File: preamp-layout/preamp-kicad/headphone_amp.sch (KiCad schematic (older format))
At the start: 34 parts, among them J72 Conn_01x04_Male, J73 Conn_01x02_Male, J74 Conn_01x02_Male, J75 Conn_01x03_Male, J76 Conn_01x03_Male, J77 Conn_01x03_Male, J78 Conn_01x03_Female, J79 Conn_01x04_Male, U19 TL072, U20 TPA6120

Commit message: Schematic Updates
Updated pin connections for DAC, footprint updates, MCU connections.
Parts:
- C41, C42, C43, C44: footprint (none) -> Capacitor_SMD:C_0805_2012Metric_Pad1.15x1.40mm_HandSolder
- J72, J79: footprint (none) -> Connector_PinHeader_2.54mm:PinHeader_1x04_P2.54mm_Vertical
- J75, J78: footprint (none) -> Connector_PinHeader_2.54mm:PinHeader_1x03_P2.54mm_Vertical
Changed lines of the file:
@@
 F 0 "C41" H 5815 2546 50  0000 L CNN
 F 1 "0.001uF" H 5815 2455 50  0000 L CNN
-F 2 "" H 5738 2350 50  0001 C CNN
+F 2 "Capacitor_SMD:C_0805_2012Metric_Pad1.15x1.40mm_HandSolder" H 5738 2350 50  0001 C CNN
 F 3 "~" H 5700 2500 50  0001 C CNN
 	1    5700 2500
@@
 F 0 "C43" V 6302 2200 50  0000 C CNN
 F 1 "0.1uF" V 6211 2200 50  0000 C CNN
-F 2 "" H 6088 2050 50  0001 C CNN
+F 2 "Capacitor_SMD:C_0805_2012Metric_Pad1.15x1.40mm_HandSolder" H 6088 2050 50  0001 C CNN
 F 3 "~" H 6050 2200 50  0001 C CNN
 	1    6050 2200
@@
 F 0 "J75" H 2422 4478 50  0000 R CNN
 F 1 "Conn_01x03_Male" H 2422 4433 50  0001 R CNN
-F 2 "" H 2450 4500 50  0001 C CNN
+F 2 "Connector_PinHeader_2.54mm:PinHeader_1x03_P2.54mm_Vertical" H 2450 4500 50  0001 C CNN
 F 3 "~" H 2450 4500 50  0001 C CNN
 	1    2450 4500
@@
 F 0 "C42" H 5815 4646 50  0000 L CNN
 F 1 "0.001uF" H 5815 4555 50  0000 L CNN
-F 2 "" H 5738 4450 50  0001 C CNN
+F 2 "Capacitor_SMD:C_0805_2012Metric_Pad1.15x1.40mm_HandSolder" H 5738 4450 50  0001 C CNN
 F 3 "~" H 5700 4600 50  0001 C CNN
 	1    5700 4600
@@
 F 0 "C44" V 6302 4300 50  0000 C CNN
 F 1 "0.1uF" V 6211 4300 50  0000 C CNN
-F 2 "" H 6088 4150 50  0001 C CNN
+F 2 "Capacitor_SMD:C_0805_2012Metric_Pad1.15x1.40mm_HandSolder" H 6088 4150 50  0001 C CNN
 F 3 "~" H 6050 4300 50  0001 C CNN
 	1    6050 4300
@@
 F 0 "J78" H 3478 4480 50  0000 L CNN
 F 1 "Conn_01x03_Female" H 3478 4435 50  0001 L CNN
-F 2 "" H 3450 4500 50  0001 C CNN
+F 2 "Connector_PinHeader_2.54mm:PinHeader_1x03_P2.54mm_Vertical" H 3450 4500 50  0001 C CNN
 F 3 "~" H 3450 4500 50  0001 C CNN
 	1    3450 4500
@@
 F 0 "J72" H 1608 2639 50  0000 C CNN
 F 1 "Conn_01x04_Male" H 1608 2640 50  0001 C CNN
-F 2 "" H 1500 2450 50  0001 C CNN
+F 2 "Connector_PinHeader_2.54mm:PinHeader_1x04_P2.54mm_Vertical" H 1500 2450 50  0001 C CNN
 F 3 "~" H 1500 2450 50  0001 C CNN
 	1    1500 2450
@@
 F 0 "J79" H 4022 2378 50  0000 R CNN
 F 1 "Conn_01x04_Male" H 4158 2640 50  0001 C CNN
-F 2 "" H 4050 2450 50  0001 C CNN
+F 2 "Connector_PinHeader_2.54mm:PinHeader_1x04_P2.54mm_Vertical" H 4050 2450 50  0001 C CNN
 F 3 "~" H 4050 2450 50  0001 C CNN
 	1    4050 2450

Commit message: Schematic Redesignation
Regenerated RefDes for all parts, updated BOM accordingly and perfomred check on values, RefDes present from schematic to BOM. Value changes, BOM filled in as a result.
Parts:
- removed J73, J74: Conn_01x02_Male, Connector_JST:JST_EH_B2B-EH-A_1x02_P2.50mm_Vertical, symbol Connector:Conn_01x02_Male
- removed J79: Conn_01x04_Male, Connector_PinHeader_2.54mm:PinHeader_1x04_P2.54mm_Vertical, symbol Connector:Conn_01x04_Male
- added J77: Conn_01x04_Female, Connector_PinHeader_2.54mm:PinHeader_1x04_P2.54mm_Vertical, symbol Connector:Conn_01x04_Female
- R62, R63: value 1.3k -> 1.5k
- renumbered J76 to J73, J77 to J74, J78 to J76
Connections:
- net GND: now also J77.2 (Pin_2)
- net xfeed_out_l: now also J77.1 (Pin_1)
- net xfeed_out_r: now also J77.3 (Pin_3)
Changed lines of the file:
@@
 Text HLabel 2150 4300 0    50   UnSpc ~ 0
 L_IN
-$Comp
-L Connector:Conn_01x02_Male J?
-U 1 1 60B7C07D
-P 1950 6100
-AR Path="/5E5EF2D4/60B7C07D" Ref="J?"  Part="1"
-AR Path="/6009D432/60B7C07D" Ref="J?"  Part="1"
-AR Path="/5E4A803E/60B7C07D" Ref="J73"  Part="1"
-F 0 "J73" H 1922 6028 50  0000 R CNN
-F 1 "Conn_01x02_Male" H 1922 5983 50  0001 R CNN
-F 2 "Connector_JST:JST_EH_B2B-EH-A_1x02_P2.50mm_Vertical" H 1950 6100 50  0001 C CNN
-F 3 "~" H 1950 6100 50  0001 C CNN
-	1    1950 6100
-	-1   0    0    -1
-$EndComp
-Text GLabel 1550 6100 0    50   UnSpc ~ 0
-+5V
-Wire Wire Line
-	1750 6200 1550 6200
-Wire Wire Line
-	1550 6200 1550 6300
-Wire Wire Line
-	1750 6100 1550 6100
-$Comp
-L power:GND #PWR?
-U 1 1 64EC0170
-P 1550 6300
-AR Path="/5E26F6FE/64EC0170" Ref="#PWR?"  Part="1"
-AR Path="/5E4A803E/64EC0170" Ref="#PWR097"  Part="1"
-F 0 "#PWR097" H 1550 6050 50  0001 C CNN
-F 1 "GND" H 1555 6127 50  0000 C CNN
-F 2 "" H 1550 6300 50  0001 C CNN
-F 3 "" H 1550 6300 50  0001 C CNN
-	1    1550 6300
-	1    0    0    -1
-$EndComp
 Text GLabel 3850 6100 1    50   UnSpc ~ 0
 +15V
@@
 AR Path="/5E4A803E/5E3C1B26" Ref="R62"  Part="1"
 F 0 "R62" H 3920 6396 50  0000 L CNN
-F 1 "1.3k" H 3920 6305 50  0000 L CNN
+F 1 "1.5k" H 3920 6305 50  0000 L CNN
 F 2 "Resistor_SMD:R_1206_3216Metric_Pad1.42x1.75mm_HandSolder" V 3780 6350 50  0001 C CNN
 F 3 "~" H 3850 6350 50  0001 C CNN
@@
 AR Path="/5E4A803E/5E3C1B36" Ref="R63"  Part="1"
 F 0 "R63" H 4470 6396 50  0000 L CNN
-F 1 "1.3k" H 4470 6305 50  0000 L CNN
+F 1 "1.5k" H 4470 6305 50  0000 L CNN
 F 2 "Resistor_SMD:R_1206_3216Metric_Pad1.42x1.75mm_HandSolder" V 4330 6350 50  0001 C CNN
 F 3 "~" H 4400 6350 50  0001 C CNN
@@
 AR Path="/5E27B612/647A3EBE" Ref="J?"  Part="1"
 AR Path="/6009D432/647A3EBE" Ref="J?"  Part="1"
-AR Path="/5E4A803E/647A3EBE" Ref="J76"  Part="1"
-F 0 "J76" H 2922 6178 50  0000 R CNN
+AR Path="/5E4A803E/647A3EBE" Ref="J73"  Part="1"
+F 0 "J73" H 2922 6178 50  0000 R CNN
 F 1 "Conn_01x03_Male" H 2922 6133 50  0001 R CNN
 F 2 "Connector_JST:JST_EH_B3B-EH-A_1x03_P2.50mm_Vertical" H 2950 6200 50  0001 C CNN
@@
 AR Path="/5E2D8DA2/5F33E58A" Ref="J?"  Part="1"
 AR Path="/6009D432/5F33E58A" Ref="J?"  Part="1"
-AR Path="/5E4A803E/5F33E58A" Ref="J78"  Part="1"
-F 0 "J78" H 3478 4480 50  0000 L CNN
+AR Path="/5E4A803E/5F33E58A" Ref="J76"  Part="1"
+F 0 "J76" H 3478 4480 50  0000 L CNN
 F 1 "Conn_01x03_Female" H 3478 4435 50  0001 L CNN
 F 2 "Connector_PinHeader_2.54mm:PinHeader_1x03_P2.54mm_Vertical" H 3450 4500 50  0001 C CNN
@@
 Text GLabel 1700 2650 2    50   UnSpc ~ 0
 -15V
-$Comp
-L Connector:Conn_01x04_Male J79
-U 1 1 5E709DB6
-P 4050 2450
-F 0 "J79" H 4022 2378 50  0000 R CNN
-F 1 "Conn_01x04_Male" H 4158 2640 50  0001 C CNN
-F 2 "Connector_PinHeader_2.54mm:PinHeader_1x04_P2.54mm_Vertical" H 4050 2450 50  0001 C CNN
-F 3 "~" H 4050 2450 50  0001 C CNN
-	1    4050 2450
-	-1   0    0    -1
-$EndComp
 NoConn ~ 3850 2650
 $Comp
@@
 Text GLabel 6200 6850 3    50   UnSpc ~ 0
 -15V
-$Comp
-L Connector:Conn_01x02_Male J?
-U 1 1 5E79808C
-P 1950 6700
-AR Path="/5E5EF2D4/5E79808C" Ref="J?"  Part="1"
-AR Path="/6009D432/5E79808C" Ref="J?"  Part="1"
-AR Path="/5E4A803E/5E79808C" Ref="J74"  Part="1"
-F 0 "J74" H 1922 6628 50  0000 R CNN
-F 1 "Conn_01x02_Male" H 1922 6583 50  0001 R CNN
-F 2 "Connector_JST:JST_EH_B2B-EH-A_1x02_P2.50mm_Vertical" H 1950 6700 50  0001 C CNN
-F 3 "~" H 1950 6700 50  0001 C CNN
-	1    1950 6700
-	-1   0    0    -1
-$EndComp
-Text GLabel 1550 6700 0    50   UnSpc ~ 0
-+5V
-Wire Wire Line
-	1750 6800 1550 6800
-Wire Wire Line
-	1550 6800 1550 6900
-Wire Wire Line
-	1750 6700 1550 6700
-$Comp
-L power:GND #PWR?
-U 1 1 5E798096
-P 1550 6900
-AR Path="/5E26F6FE/5E798096" Ref="#PWR?"  Part="1"
-AR Path="/5E4A803E/5E798096" Ref="#PWR098"  Part="1"
-F 0 "#PWR098" H 1550 6650 50  0001 C CNN
-F 1 "GND" H 1555 6727 50  0000 C CNN
-F 2 "" H 1550 6900 50  0001 C CNN
-F 3 "" H 1550 6900 50  0001 C CNN
-	1    1550 6900
-	1    0    0    -1
-$EndComp
 $Comp
 L power:GND #PWR?
@@
 AR Path="/5E27B612/5E7A75D4" Ref="J?"  Part="1"
 AR Path="/6009D432/5E7A75D4" Ref="J?"  Part="1"
-AR Path="/5E4A803E/5E7A75D4" Ref="J77"  Part="1"
-F 0 "J77" H 2922 6778 50  0000 R CNN
+AR Path="/5E4A803E/5E7A75D4" Ref="J74"  Part="1"
+F 0 "J74" H 2922 6778 50  0000 R CNN
 F 1 "Conn_01x03_Male" H 2922 6733 50  0001 R CNN
 F 2 "Connector_JST:JST_EH_B3B-EH-A_1x03_P2.50mm_Vertical" H 2950 6800 50  0001 C CNN
@@
 Text GLabel 2650 6600 0    50   UnSpc ~ 0
 +15V
+$Comp
+L Connector:Conn_01x04_Female J77
+U 1 1 5EF5CC6D
+P 4050 2450
+F 0 "J77" H 4078 2380 50  0000 L CNN
+F 1 "Conn_01x04_Female" H 4078 2335 50  0001 L CNN
+F 2 "Connector_PinHeader_2.54mm:PinHeader_1x04_P2.54mm_Vertical" H 4050 2450 50  0001 C CNN
+F 3 "~" H 4050 2450 50  0001 C CNN
+	1    4050 2450
+	1    0    0    -1
+$EndComp
 $EndSCHEMATC

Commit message: Added Bypass Capacitors
0.1uF caps added at power supplies of all ICs
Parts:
- added C61, C62, C63, C64, C65, C66: 0.1uF, Capacitor_SMD:C_0805_2012Metric_Pad1.15x1.40mm_HandSolder, symbol Device:C
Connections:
- net +15V: now also C61.1, C63.1, C65.1
- net -15V: now also C62.1, C64.1, C66.1
- net GND: now also C61.2, C62.2, C63.2, C64.2, C65.2, C66.2
- net at R72.1, R76.2: now also U20.5 (-); no longer U20.4 (+)
- net at R74.1: now also U20.4 (+); no longer U20.5 (-)
- net at U20.16 (-): now also R73.1, R77.2; no longer R75.1
- new net: R75.1, U20.17 (+)
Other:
- moved on the sheet: C41, C42, C43, C44, D57, D58, J73, J74, R62, R63, R64, R65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

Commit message: Footprint assignment updates
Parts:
- U19: footprint (none) -> Package_DIP:DIP-8_W7.62mm_Socket_LongPads
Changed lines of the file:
@@
 F 0 "U19" H 3908 6596 50  0000 L CNN
 F 1 "TL072" H 3908 6505 50  0000 L CNN
-F 2 "" H 3950 6550 50  0001 C CNN
+F 2 "Package_DIP:DIP-8_W7.62mm_Socket_LongPads" H 3950 6550 50  0001 C CNN
 F 3 "http://www.ti.com/lit/ds/symlink/tl071.pdf" H 3950 6550 50  0001 C CNN
 	3    3950 6550

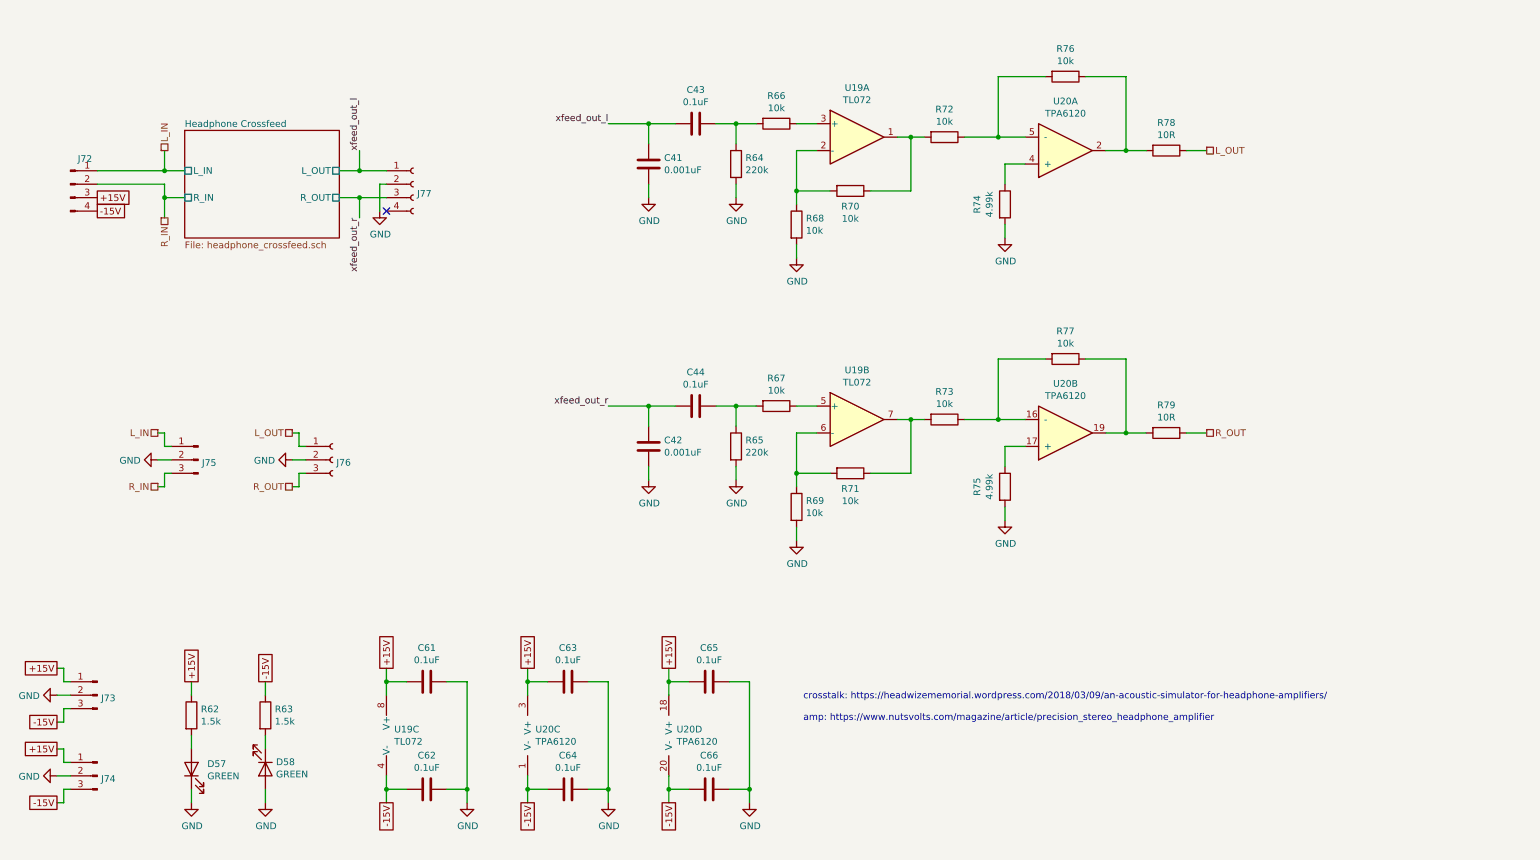
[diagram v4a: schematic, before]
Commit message: Headphone Amp Update
Removed IC buffer on headphone amp schematic. Reconfigured connectors to crossfeed board so that input/output can be easily jumpered.
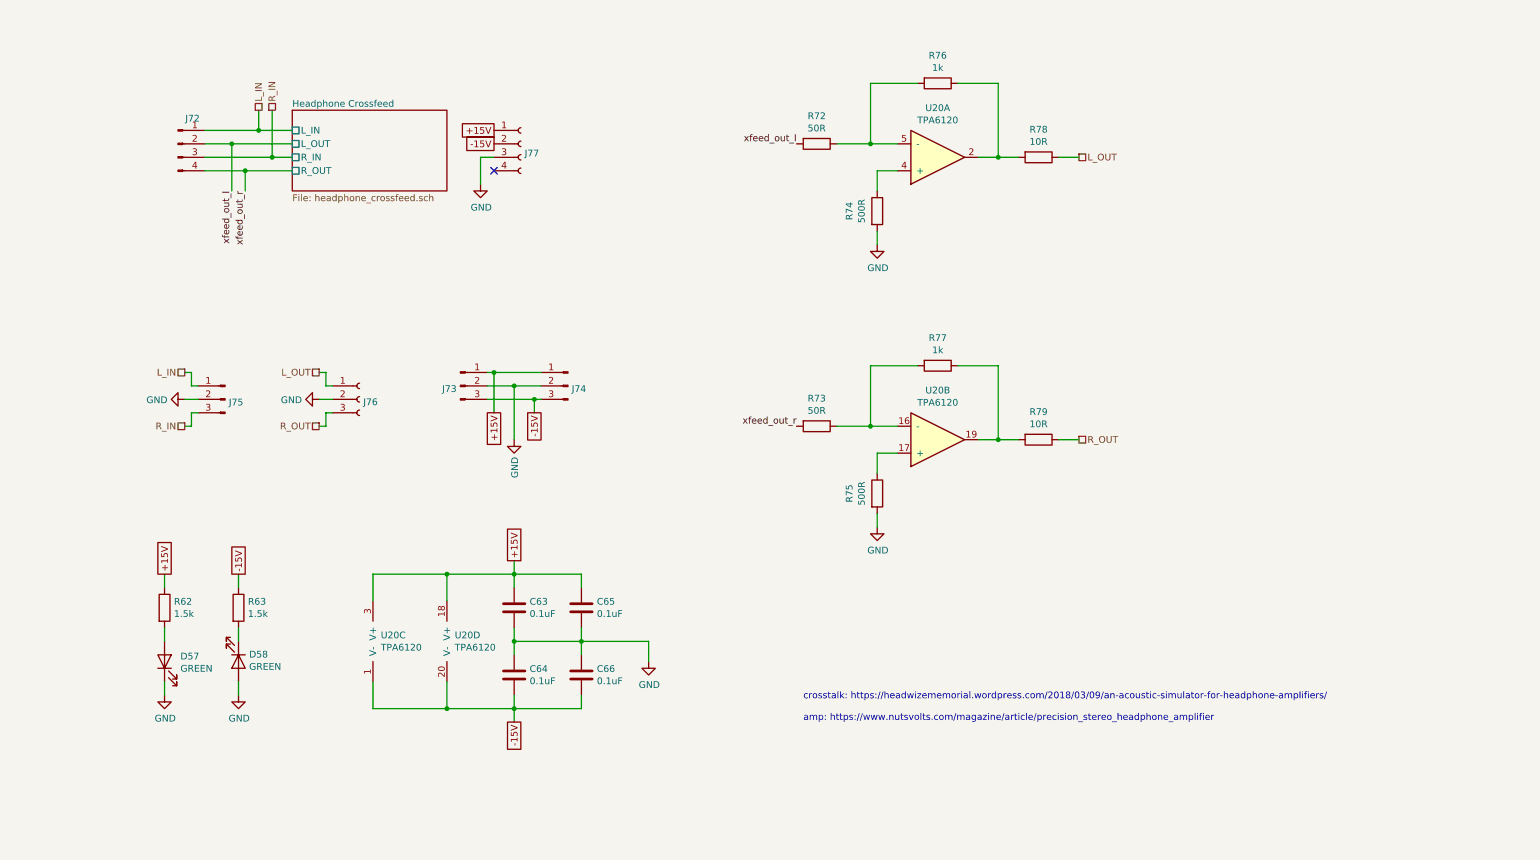
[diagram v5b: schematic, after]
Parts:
- removed C41, C42: 0.001uF, Capacitor_SMD:C_0805_2012Metric_Pad1.15x1.40mm_HandSolder, symbol Device:C
- removed C43, C44, C61, C62: 0.1uF, Capacitor_SMD:C_0805_2012Metric_Pad1.15x1.40mm_HandSolder, symbol Device:C
- removed R64, R65: 220k, Resistor_SMD:R_1206_3216Metric_Pad1.42x1.75mm_HandSolder, symbol Device:R
- removed R66, R67, R68, R69, R70, R71: 10k, Resistor_SMD:R_1206_3216Metric_Pad1.42x1.75mm_HandSolder, symbol Device:R
- removed U19: TL072, Package_DIP:DIP-8_W7.62mm_Socket_LongPads, symbol Amplifier_Operational:TL072
- R72, R73: value 10k -> 50R
- R74, R75: value 4.99k -> 500R
- R76, R77: value 10k -> 1k
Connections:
- net +15V: now also J77.1 (Pin_1); no longer J72.3 (Pin_3)
- net -15V: now also C66.2, J77.2 (Pin_2); no longer C66.1, J72.4 (Pin_4)
- net GND: now also C66.1, J77.3 (Pin_3); no longer C66.2, J77.2 (Pin_2)
- net R_IN: now also J72.3 (Pin_3); no longer J72.2 (Pin_2)
- net xfeed_out_l: now also J72.2 (Pin_2), R72.2; no longer J77.1 (Pin_1)
- net xfeed_out_r: now also J72.4 (Pin_4), R73.2; no longer J77.3 (Pin_3)
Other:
- moved on the sheet: C63, C64, C65, C66, D57, D58, J72, J73, J74, J75, J76, J77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

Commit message: Footprint updates
Footprint creation of relay, ESP32
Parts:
- U20: footprint (none) -> Package_SO:SOIC-20W_7.5x12.8mm_P1.27mm
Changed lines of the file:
@@
 F 0 "U20" H 3808 5896 50  0000 L CNN
 F 1 "TPA6120" H 3808 5805 50  0000 L CNN
-F 2 "" H 3900 6100 50  0001 C CNN
+F 2 "Package_SO:SOIC-20W_7.5x12.8mm_P1.27mm" H 3900 6100 50  0001 C CNN
 F 3 "" H 3900 6100 50  0001 C CNN
 	3    3850 5850
@@
 F 0 "U20" H 4358 5896 50  0000 L CNN
 F 1 "TPA6120" H 4358 5805 50  0000 L CNN
-F 2 "" H 4450 6100 50  0001 C CNN
+F 2 "Package_SO:SOIC-20W_7.5x12.8mm_P1.27mm" H 4450 6100 50  0001 C CNN
 F 3 "" H 4450 6100 50  0001 C CNN
 	4    4400 5850
@@
 F 0 "U20" H 7950 3983 50  0000 C CNN
 F 1 "TPA6120" H 7950 4074 50  0000 C CNN
-F 2 "" H 8000 4600 50  0001 C CNN
+F 2 "Package_SO:SOIC-20W_7.5x12.8mm_P1.27mm" H 8000 4600 50  0001 C CNN
 F 3 "" H 8000 4600 50  0001 C CNN
 	2    7950 4350
@@
 F 0 "U20" H 7950 1883 50  0000 C CNN
 F 1 "TPA6120" H 7950 1974 50  0000 C CNN
-F 2 "" H 8000 2500 50  0001 C CNN
+F 2 "Package_SO:SOIC-20W_7.5x12.8mm_P1.27mm" H 8000 2500 50  0001 C CNN
 F 3 "" H 8000 2500 50  0001 C CNN
 	1    7950 2250
@@
 P 4800 4350
 AR Path="/6009D432/601F478F" Ref="#PWR?"  Part="1"
-AR Path="/5E4A803E/601F478F" Ref="#PWR?"  Part="1"
-F 0 "#PWR?" H 4800 4100 50  0001 C CNN
+AR Path="/5E4A803E/601F478F" Ref="#PWR0106"  Part="1"
+F 0 "#PWR0106" H 4800 4100 50  0001 C CNN
 F 1 "GND" V 4805 4222 50  0000 R CNN
 F 2 "" H 4800 4350 50  0001 C CNN
